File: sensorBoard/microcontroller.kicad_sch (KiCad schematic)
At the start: 20 parts, among them U23 STM32L476RGTx, Y2 8MHz

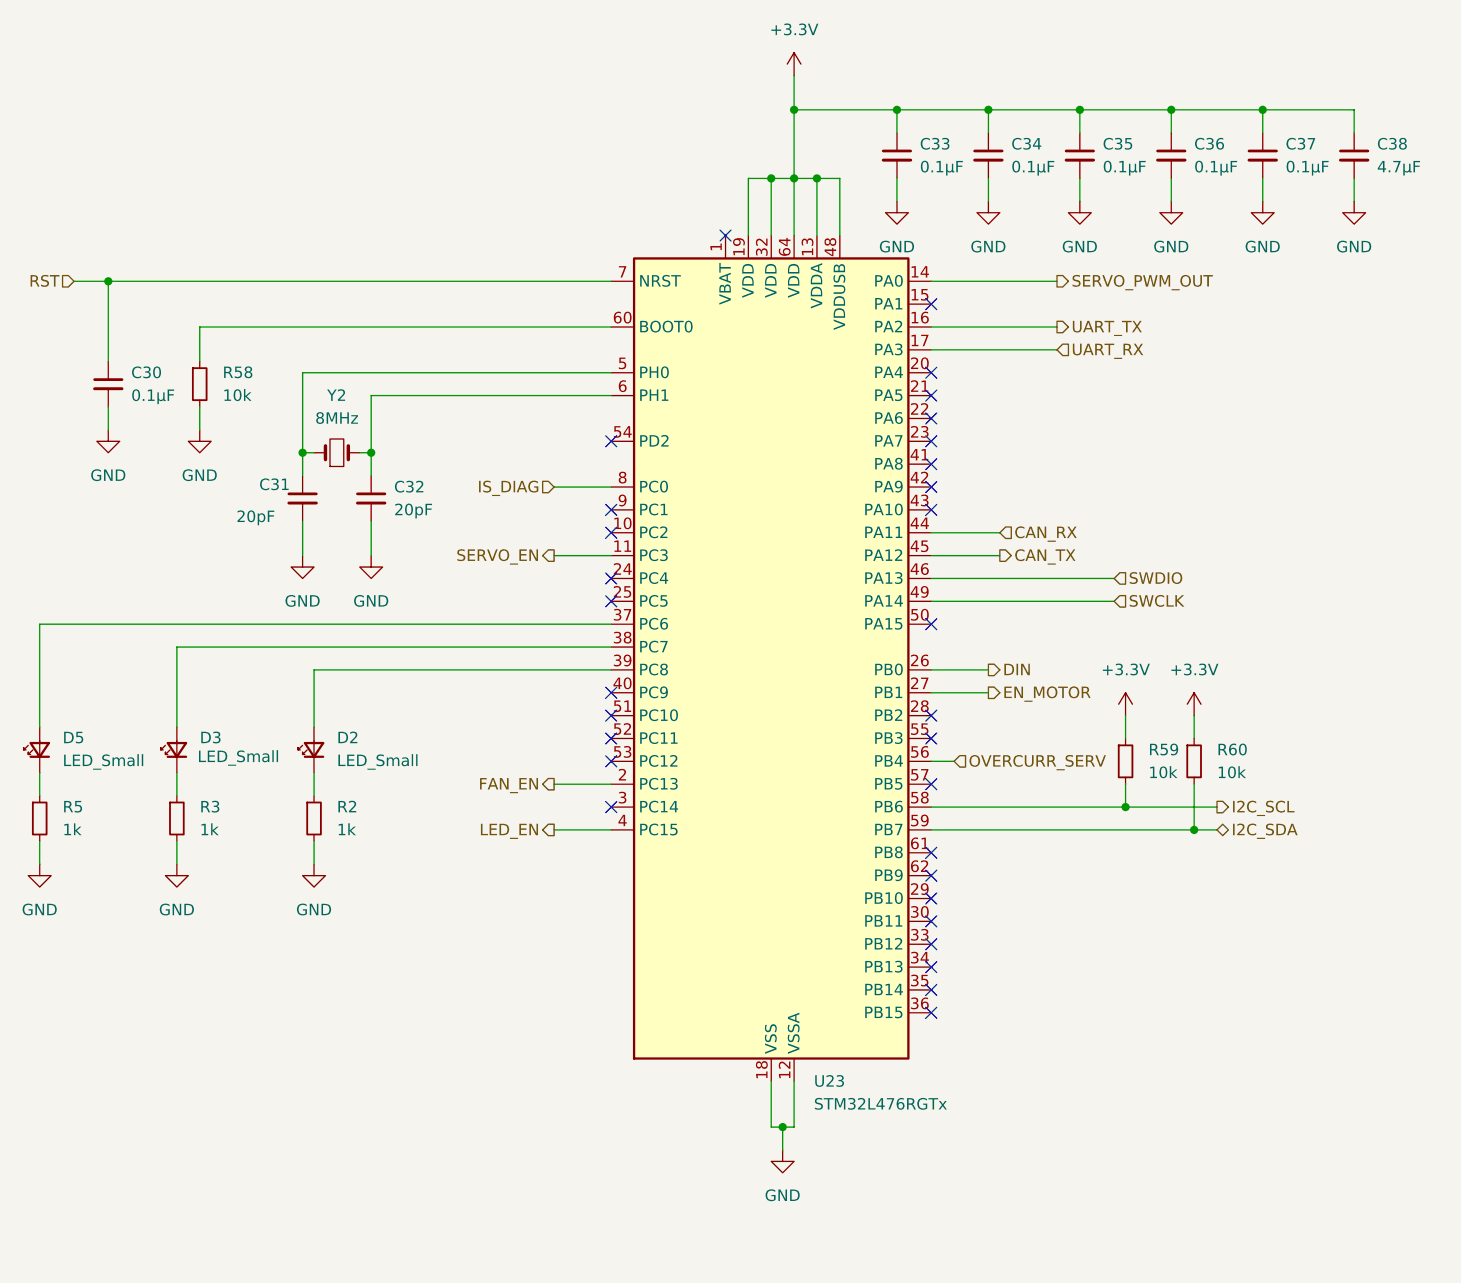
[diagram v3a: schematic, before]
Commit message: Das erstes PCB ist fast fertig. Die Vias waren auf die Platine platziert und Poligon war gefüllt.
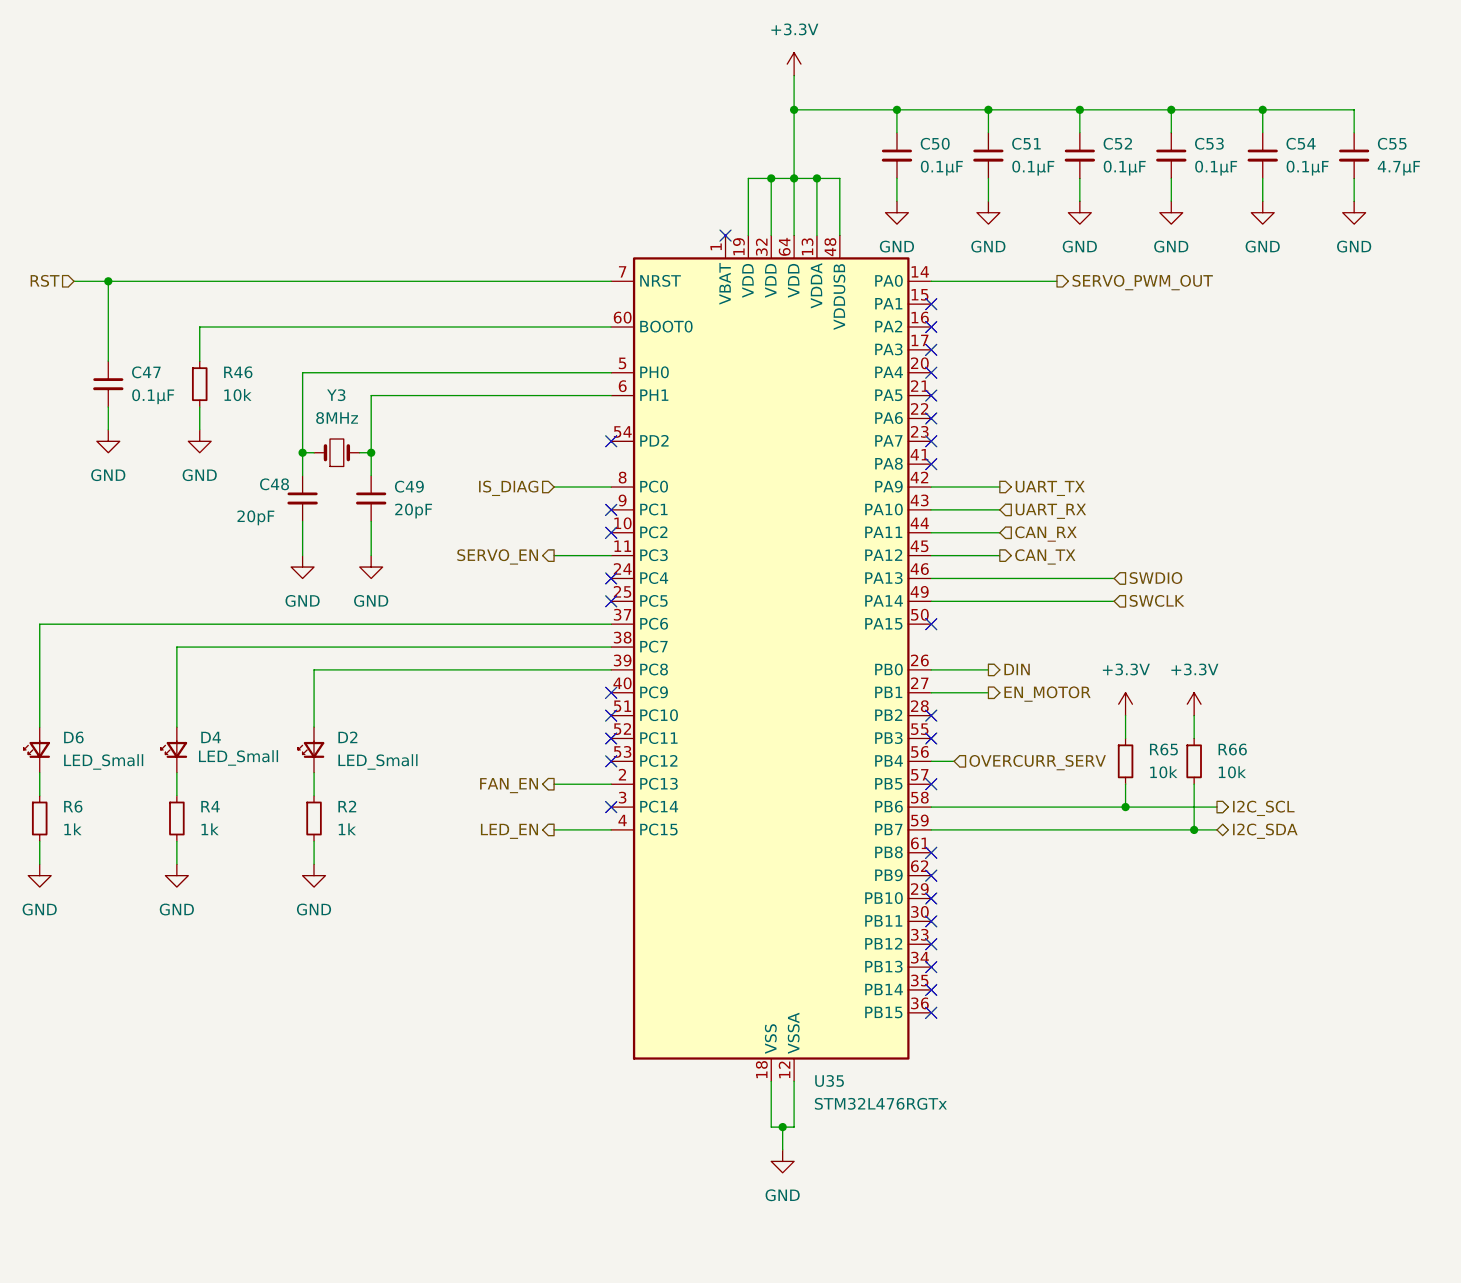
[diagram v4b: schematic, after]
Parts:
- renumbered C30 to C47, C31 to C48, C32 to C49, C33 to C50, C34 to C51, C35 to C52, C36 to C53, C37 to C54, C38 to C55, D3 to D4, D5 to D6, R3 to R4, R58 to R46, R5 to R6, R59 to R65, R60 to R66, U23 to U35, Y2 to Y3
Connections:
- net UART_RX: now also U35.43 (PA10); no longer U35.17 (PA3)
- net UART_TX: now also U35.42 (PA9); no longer U35.16 (PA2)
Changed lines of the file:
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@@
 	)
 	(no_connect
-		(at 147.32 60.96)
+		(at 147.32 53.34)
 	)
 	(no_connect
-		(at 147.32 114.3)
+		(at 147.32 60.96)
 	)
 	(no_connect
-		(at 147.32 71.12)
+		(at 147.32 114.3)
 	)
 	(no_connect
@@
 	)
 	(no_connect
+		(at 147.32 50.8)
+	)
+	(no_connect
 		(at 147.32 109.22)
 	)
@@
 	)
 	(no_connect
-		(at 147.32 68.58)
-	)
-	(no_connect
 		(at 147.32 83.82)
 	)
@@
 	(wire
 		(pts
-			(xy 147.32 50.8) (xy 161.29 50.8)
-		)
-		(stroke
-			(width 0)
-			(type default)
-		)
-	)
-	(wire
-		(pts
 			(xy 147.32 106.68) (xy 176.53 106.68)
 		)
@@
 	(wire
 		(pts
+			(xy 147.32 68.58) (xy 154.94 68.58)
+		)
+		(stroke
+			(width 0)
+			(type default)
+		)
+	)
+	(wire
+		(pts
 			(xy 147.32 76.2) (xy 154.94 76.2)
 		)
@@
 	(wire
 		(pts
+			(xy 147.32 71.12) (xy 154.94 71.12)
+		)
+		(stroke
+			(width 0)
+			(type default)
+		)
+	)
+	(wire
+		(pts
 			(xy 63.5 86.36) (xy 111.76 86.36)
 		)
@@
 	(wire
 		(pts
-			(xy 147.32 53.34) (xy 161.29 53.34)
-		)
-		(stroke
-			(width 0)
-			(type default)
-		)
-	)
-	(wire
-		(pts
 			(xy 176.53 101.6) (xy 176.53 106.68)
 		)
@@
 	(hierarchical_label "UART_RX"
 		(shape input)
-		(at 161.29 53.34 0)
+		(at 154.94 71.12 0)
 		(fields_autoplaced yes)
 		(effects
@@
 	(hierarchical_label "UART_TX"
 		(shape output)
-		(at 161.29 50.8 0)
+		(at 154.94 68.58 0)
 		(fields_autoplaced yes)
 		(effects
@@
 		(dnp no)
 		(fields_autoplaced yes)
-		(property "Reference" "#PWR03"
+		(property "Reference" "#PWR04"
 			(at 63.5 116.84 0)
 			(effects
@@
 		(dnp no)
 		(fields_autoplaced yes)
-		(property "Reference" "#PWR05"
+		(property "Reference" "#PWR06"
 			(at 48.26 116.84 0)
 			(effects
@@
 		(dnp no)
 		(fields_autoplaced yes)
-		(property "Reference" "#PWR0157"
+		(property "Reference" "#PWR0239"
 			(at 173.99 43.18 0)
 			(effects
@@
 		(dnp no)
 		(fields_autoplaced yes)
-		(property "Reference" "#PWR0154"
+		(property "Reference" "#PWR0236"
 			(at 153.67 43.18 0)
 			(effects
@@
 		(dnp no)
 		(fields_autoplaced yes)
-		(property "Reference" "U23"
+		(property "Reference" "U35"
 			(at 134.2741 134.62 0)
 			(effects
@@
 		(dnp no)
 		(fields_autoplaced yes)
-		(property "Reference" "R5"
+		(property "Reference" "R6"
 			(at 50.8 104.1399 0)
 			(effects
@@
 		(dnp no)
 		(fields_autoplaced yes)
-		(property "Reference" "C32"
+		(property "Reference" "C49"
 			(at 87.63 68.5862 0)
 			(effects
@@
 		(dnp no)
 		(fields_autoplaced yes)
-		(property "Reference" "C34"
+		(property "Reference" "C51"
 			(at 156.21 30.4862 0)
 			(effects
@@
 		(dnp no)
 		(fields_autoplaced yes)
-		(property "Reference" "C30"
+		(property "Reference" "C47"
 			(at 58.42 55.8862 0)
 			(effects
@@
 		(dnp no)
 		(fields_autoplaced yes)
-		(property "Reference" "C36"
+		(property "Reference" "C53"
 			(at 176.53 30.4862 0)
 			(effects
@@
 		(dnp no)
 		(fields_autoplaced yes)
-		(property "Reference" "#PWR0148"
+		(property "Reference" "#PWR0230"
 			(at 66.04 68.58 0)
 			(effects
@@
 		(dnp no)
 		(fields_autoplaced yes)
-		(property "Reference" "#PWR0160"
+		(property "Reference" "#PWR0242"
 			(at 194.31 43.18 0)
 			(effects
@@
 		(dnp no)
 		(fields_autoplaced yes)
-		(property "Reference" "#PWR0147"
+		(property "Reference" "#PWR0229"
 			(at 55.88 68.58 0)
 			(effects
@@
 		(dnp no)
 		(fields_autoplaced yes)
-		(property "Reference" "#PWR0158"
+		(property "Reference" "#PWR0240"
 			(at 176.53 97.79 0)
 			(effects
@@
 		(dnp no)
 		(fields_autoplaced yes)
-		(property "Reference" "C33"
+		(property "Reference" "C50"
 			(at 146.05 30.4862 0)
 			(effects
@@
 		(dnp no)
 		(fields_autoplaced yes)
-		(property "Reference" "#PWR0153"
+		(property "Reference" "#PWR0235"
 			(at 143.51 43.18 0)
 			(effects
@@
 		(dnp no)
 		(fields_autoplaced yes)
-		(property "Reference" "#PWR0159"
+		(property "Reference" "#PWR0241"
 			(at 184.15 43.18 0)
 			(effects
@@
 		(dnp no)
 		(fields_autoplaced yes)
-		(property "Reference" "D5"
+		(property "Reference" "D6"
 			(at 50.8 96.4564 90)
 			(effects
@@
 		(dnp no)
 		(fields_autoplaced yes)
-		(property "Reference" "R3"
+		(property "Reference" "R4"
 			(at 66.04 104.1399 0)
 			(effects
@@
 		(dnp no)
 		(fields_autoplaced yes)
-		(property "Reference" "#PWR0152"
+		(property "Reference" "#PWR0234"
 			(at 132.08 26.67 0)
 			(effects
@@
 		(dnp no)
 		(fields_autoplaced yes)
-		(property "Reference" "#PWR0156"
+		(property "Reference" "#PWR0238"
 			(at 168.91 97.79 0)
 			(effects
@@
 		(on_board yes)
 		(dnp no)
-		(property "Reference" "D3"
+		(property "Reference" "D4"
 			(at 66.04 96.4564 90)
 			(effects
@@
 		(dnp no)
 		(fields_autoplaced yes)
-		(property "Reference" "C38"
+		(property "Reference" "C55"
 			(at 196.85 30.4862 0)
 			(effects
@@
 		(dnp no)
 		(fields_autoplaced yes)
-		(property "Reference" "C37"
+		(property "Reference" "C54"
 			(at 186.69 30.4862 0)
 			(effects
@@
 		(dnp no)
 		(fields_autoplaced yes)
-		(property "Reference" "#PWR0149"
+		(property "Reference" "#PWR0231"
 			(at 77.47 82.55 0)
 			(effects
@@
 		(dnp no)
 		(fields_autoplaced yes)
-		(property "Reference" "R58"
+		(property "Reference" "R46"
 			(at 68.58 55.8799 0)
 			(effects
@@
 		(dnp no)
 		(fields_autoplaced yes)
-		(property "Reference" "#PWR0155"
+		(property "Reference" "#PWR0237"
 			(at 163.83 43.18 0)
 			(effects
@@
 		(dnp no)
 		(fields_autoplaced yes)
-		(property "Reference" "R60"
+		(property "Reference" "R66"
 			(at 179.07 97.7899 0)
 			(effects
@@
 		(dnp no)
 		(fields_autoplaced yes)
-		(property "Reference" "Y2"
+		(property "Reference" "Y3"
 			(at 81.28 58.42 0)
 			(effects
@@
 		(on_board yes)
 		(dnp no)
-		(property "Reference" "C31"
+		(property "Reference" "C48"
 			(at 72.644 68.326 0)
 			(effects
@@
 		(dnp no)
 		(fields_autoplaced yes)
-		(property "Reference" "#PWR0150"
+		(property "Reference" "#PWR0232"
 			(at 85.09 82.55 0)
 			(effects
@@
 		(dnp no)
 		(fields_autoplaced yes)
-		(property "Reference" "R59"
+		(property "Reference" "R65"
 			(at 171.45 97.7899 0)
 			(effects
@@
 		(dnp no)
 		(fields_autoplaced yes)
-		(property "Reference" "#PWR0151"
+		(property "Reference" "#PWR0233"
 			(at 130.81 148.59 0)
 			(effects
@@
 		(dnp no)
 		(fields_autoplaced yes)
-		(property "Reference" "C35"
+		(property "Reference" "C52"
 			(at 166.37 30.4862 0)
 			(effects

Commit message: added old software + new PCB
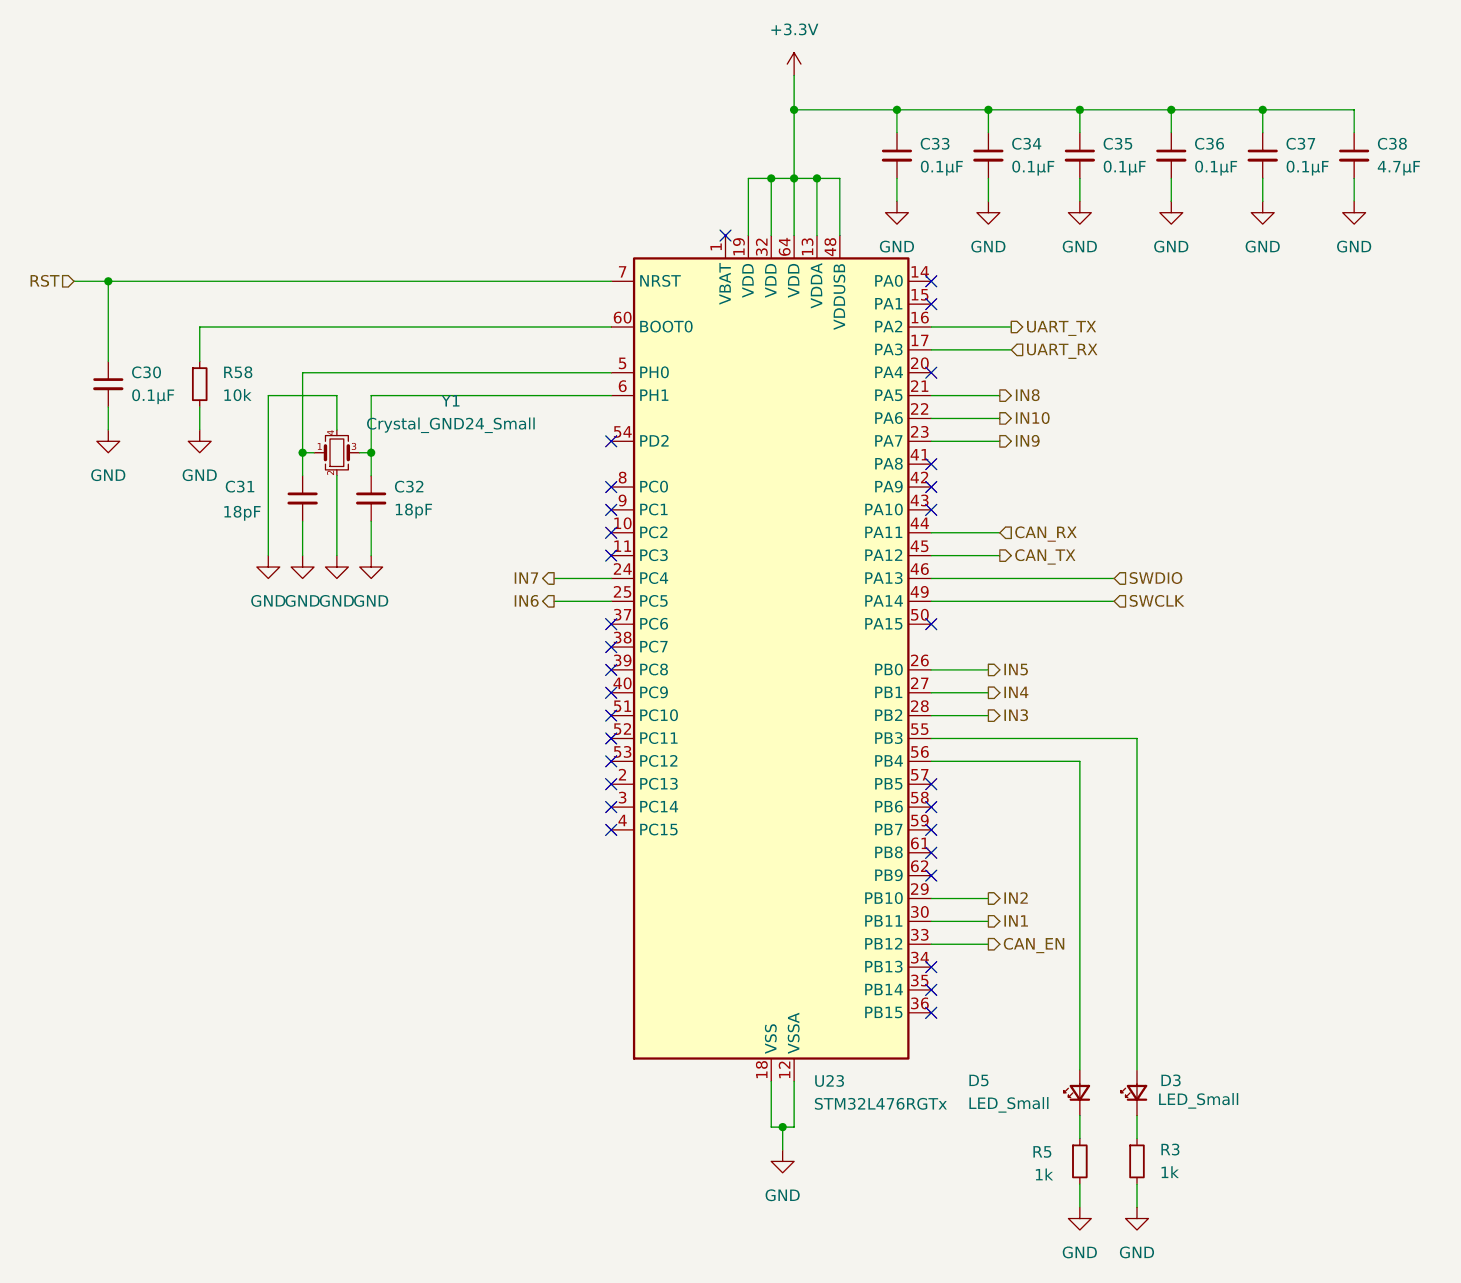
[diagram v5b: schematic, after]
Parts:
- removed D2: LED_Small, LED_SMD:LED_0805_2012Metric, symbol Device:LED_Small
- removed R2: 1k, Resistor_SMD:R_0805_2012Metric, symbol Device:R_Small
- removed R65, R66: 10k, Resistor_SMD:R_0805_2012Metric, symbol Device:R_Small
- removed Y3: 8MHz, Crystal:Crystal_SMD_HC49-SD_HandSoldering, symbol Device:Crystal_Small
- added Y1: Crystal_GND24_Small, Crystal:Crystal_SMD_3225-4Pin_3.2x2.5mm, symbol Device:Crystal_GND24_Small
- C31: renamed from C48; value 20pF -> 18pF
- C32: renamed from C49; value 20pF -> 18pF
- renumbered C47 to C30, C50 to C33, C51 to C34, C52 to C35, C53 to C36, C54 to C37, C55 to C38, D4 to D3, D6 to D5, R4 to R3, R6 to R5, R46 to R58, U35 to U23
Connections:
- net GND: now also Y1.2, Y1.4
- net UART_RX: now also U23.17 (PA3); no longer U23.43 (PA10)
- net UART_TX: now also U23.16 (PA2); no longer U23.42 (PA9)
- net IN8: now reaches U23.21 (PA5)
- net IN10: now reaches U23.22 (PA6)
- net IN9: now reaches U23.23 (PA7)
- net IN7: now reaches U23.24 (PC4)
- net IN6: now reaches U23.25 (PC5)
- net IN3: now reaches U23.28 (PB2)
- net IN2: now reaches U23.29 (PB10)
- net IN1: now reaches U23.30 (PB11)
- net CAN_EN: now reaches U23.33 (PB12)
- net at U23.37 (PC6): no longer D5.2 (A)
- net at U23.38 (PC7): no longer D3.2 (A)
- net at C31.1, U23.5 (PH0): now also Y1.1
- net at U23.55 (PB3): now also D3.2 (A)
- net at C32.1, U23.6 (PH1): now also Y1.3
- net DIN renamed IN5
- net EN_MOTOR renamed IN4
- net FAN_EN: no longer names the net of U23.2 (PC13)
- net I2C_SCL: no longer names the net of U23.58 (PB6)
- net I2C_SDA: no longer names the net of U23.59 (PB7)
- net IS_DIAG: no longer names the net of U23.8 (PC0)
- net LED_EN: no longer names the net of U23.4 (PC15)
- net OVERCURR_SERV: no longer names the net of U23.56 (PB4)
- net OVERCURR_SERV: now also D5.2 (A)
- net SERVO_EN: no longer names the net of U23.11 (PC3)
- net SERVO_PWM_OUT: no longer names the net of U23.14 (PA0)
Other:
- moved on the sheet: D3, D5, R3, R5
